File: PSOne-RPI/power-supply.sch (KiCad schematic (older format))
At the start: 16 parts, among them U1 TPS22929D, U2 MC34063AD, U3 TPS22929D

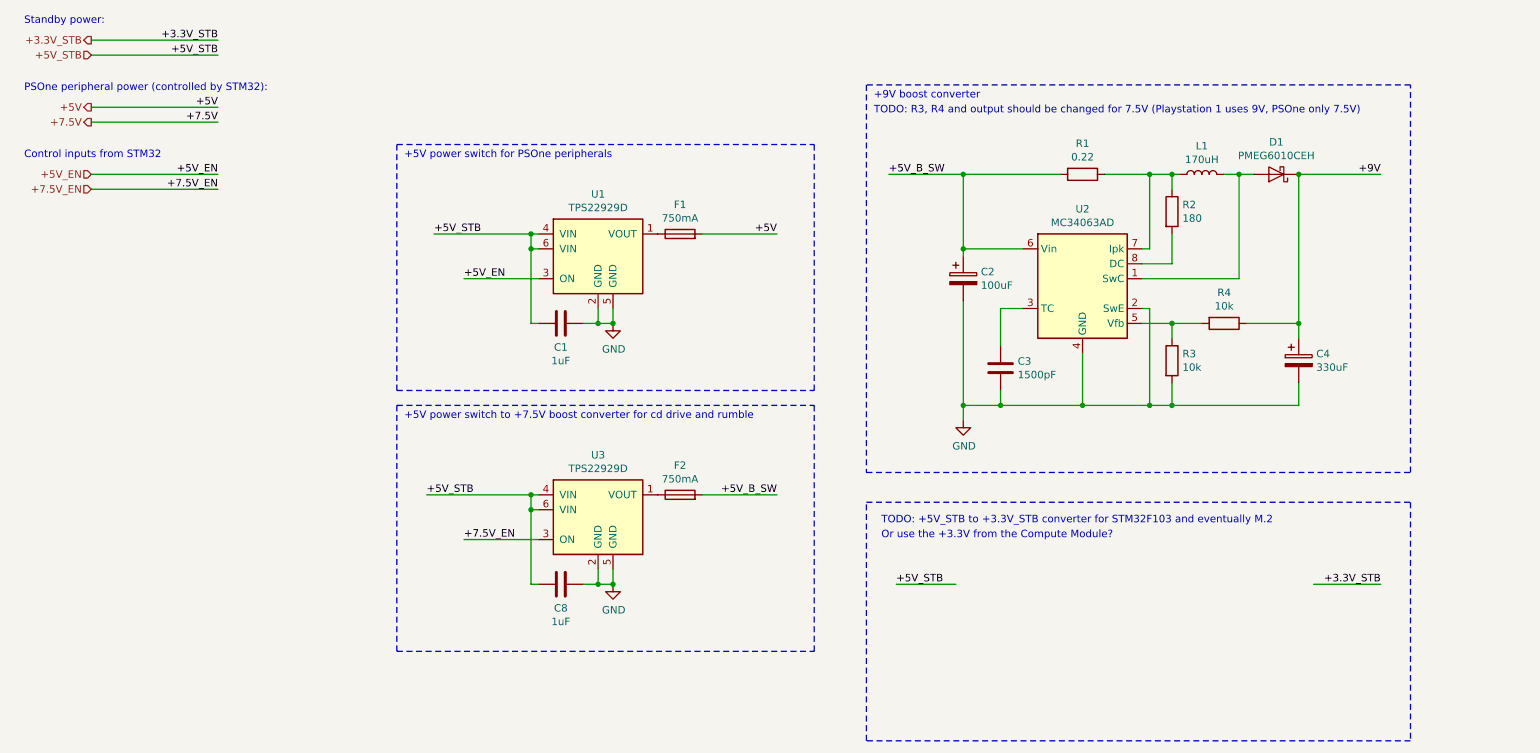
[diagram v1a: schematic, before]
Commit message: Updated internal power supply
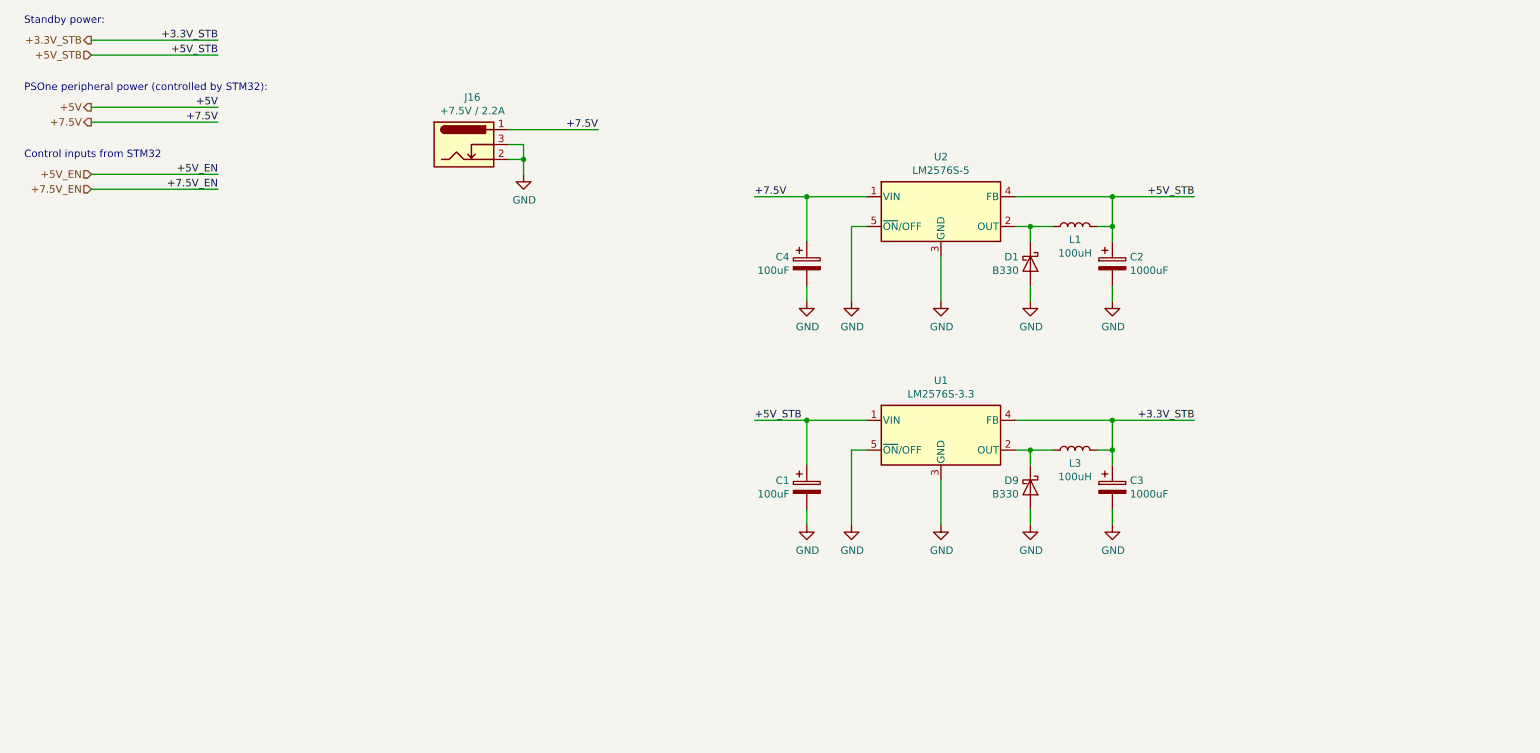
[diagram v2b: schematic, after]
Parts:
- removed C1, C8: 1uF, Capacitor_SMD:C_1206_3216Metric, symbol Device:C
- removed C3: 1500pF, Capacitor_SMD:C_1206_3216Metric, symbol Device:C
- removed D1: PMEG6010CEH, Diode_SMD:D_SOD-123, symbol Diode:PMEG6010CEH
- removed F1, F2: 750mA, Fuse:Fuse_1210_3225Metric, symbol Device:Fuse
- removed R1: 0.22, Resistor_SMD:R_1206_3216Metric, symbol Device:R
- removed R2: 180, Resistor_SMD:R_1206_3216Metric, symbol Device:R
- removed R3, R4: 10k, Resistor_SMD:R_1206_3216Metric, symbol Device:R
- removed U1, U3: TPS22929D, Package_TO_SOT_SMD:SOT-23-6, symbol Power_Management:TPS22929D
- removed U2: MC34063AD, Package_SO:SOIC-8_3.9x4.9mm_P1.27mm, symbol Regulator_Switching:MC34063AD
- added C1: 100uF, Capacitor_SMD:CP_Elec_6.3x5.8, symbol Device:CP
- added C3: 1000uF, Capacitor_SMD:CP_Elec_8x6.5, symbol Device:CP
- added D1, D9: B330, Diode_SMD:D_SMC, symbol Diode:B330
- added J16: +7.5V / 2.2A, Connector_BarrelJack:BarrelJack_Wuerth_6941xx301002, symbol Connector:Barrel_Jack_Switch
- added L3: 100uH, Inductor_SMD:L_Bourns_SRR1260, symbol Device:L
- added U1: LM2576S-3.3, Package_TO_SOT_SMD:TO-263-5_TabPin3, symbol Regulator_Switching:LM2576S-3.3
- added U2: LM2576S-5, Package_TO_SOT_SMD:TO-263-5_TabPin3, symbol Regulator_Switching:LM2576S-5
- C2: value 100uF -> 1000uF; footprint Capacitor_SMD:CP_Elec_6.3x5.9 -> Capacitor_SMD:CP_Elec_8x6.5
- C4: value 330uF -> 100uF; footprint Capacitor_SMD:CP_Elec_6.3x5.9 -> Capacitor_SMD:CP_Elec_6.3x5.8
- L1: value 170uH -> 100uH; footprint Inductor_SMD:L_TDK_SLF12575 -> Inductor_SMD:L_Bourns_SRR1260
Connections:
- net labels removed: +5V_B_SW, +9V
- wire segments 71 -> 45
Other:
- note removed: "+5V power switch for PSOne peripherals"
- note removed: "+5V power switch to +7.5V boost converter for cd drive and rumble"
- note removed: "+9V boost converter"
- note removed: "Or use the +3.3V from the Compute Module?"
- note removed: "TODO: +5V_STB to +3.3V_STB converter for STM32F103 and eventually M.2"
- note removed: "TODO: R3, R4 and output should be changed for 7.5V (Playstation 1 uses 9V, PSOne only 7.5V)"
- moved on the sheet: C2, C4
